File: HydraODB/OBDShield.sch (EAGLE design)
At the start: 29 parts, among them IC1 LM317MABDT, J1 HYDRABUS_SHIELD_CON_HEADER_2X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, J2 HYDRABUS_SHIELD_CON_HEADER_2X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, J3 HYDRABUS_SHIELD_CON_HEADER_2X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, K1 TS-1101F, U1 SN65HVD233DG4, U2 SN65HVD233DG4

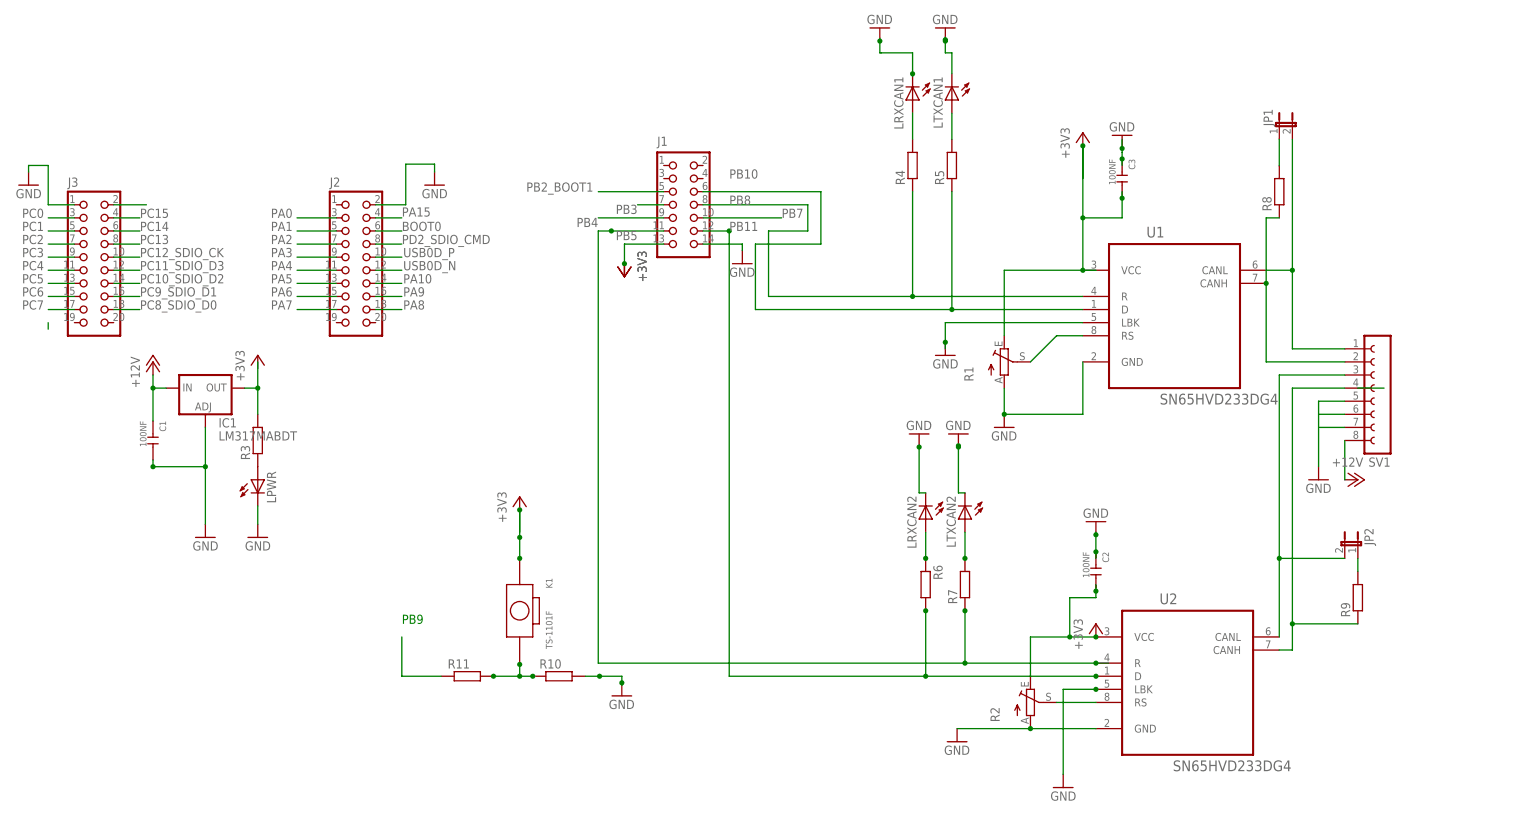
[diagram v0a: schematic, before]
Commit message: Power changed and jumper added, packages changed, inverted can h/l on silk
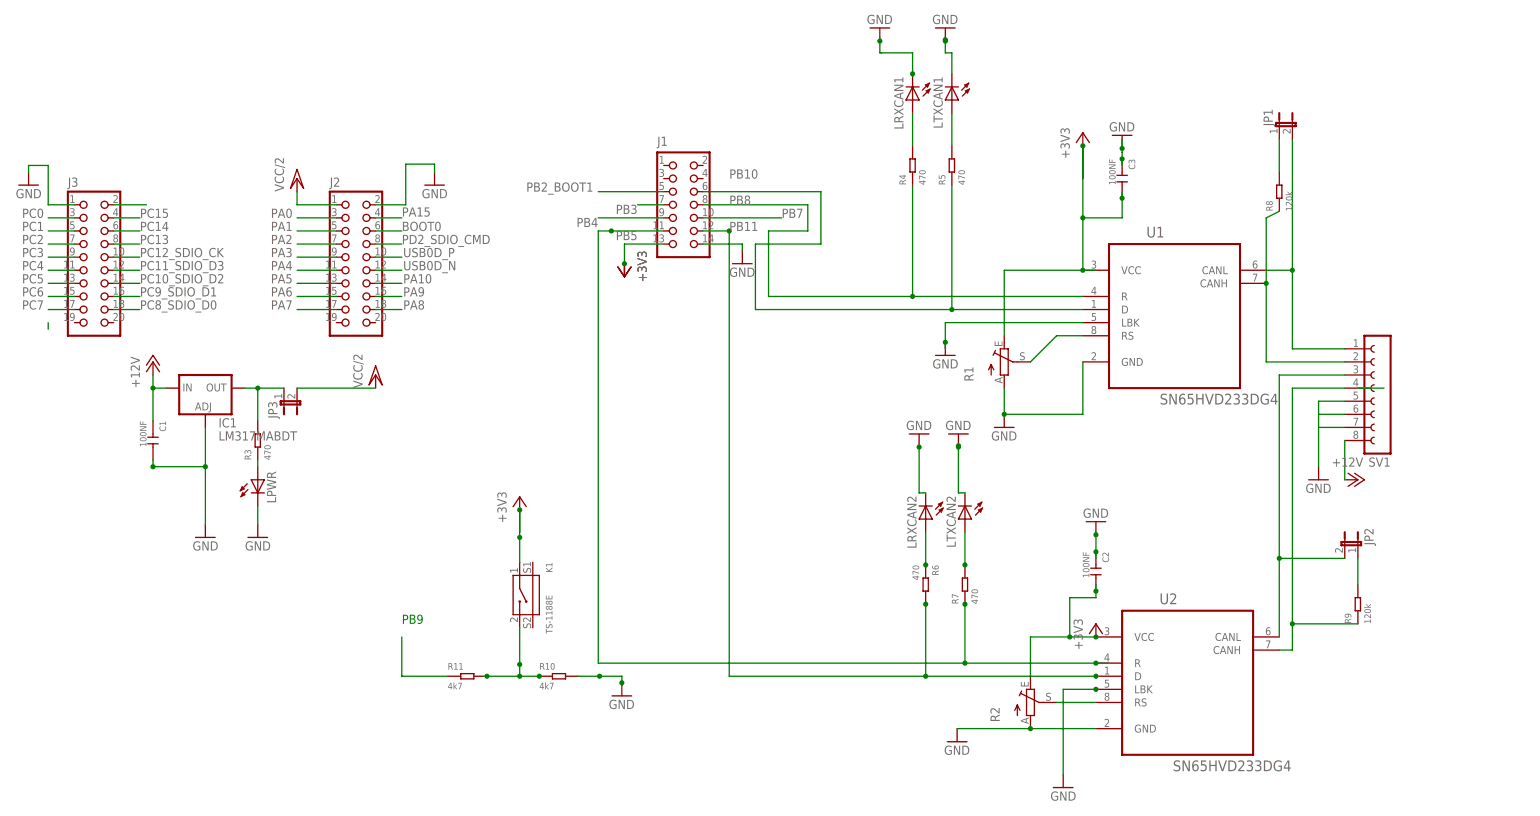
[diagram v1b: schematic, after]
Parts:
- added JP3: (no value), jumper:JP1E
- K1: value TS-1101F -> TS-1188E; device Seeed-OPL-Button:DIP-BUTTON-FRONT-WHITE(2P-3.4X6MM) -> Seeed-OPL-Button:SMD-BUTTON-2+2P
- R10, R11: value (none) -> 4k7; device resistor:R-EU_R0603 -> Seeed-OPL-Resistor:SMD-RES-33K-1%-1/4W(1206)
- R3, R4, R5, R6, R7: value (none) -> 470; device resistor:R-EU_R0603 -> Seeed-OPL-Resistor:SMD-RES-33K-1%-1/4W(1206)
- R8, R9: value (none) -> 120k; device resistor:R-EU_R0603 -> Seeed-OPL-Resistor:SMD-RES-33K-1%-1/4W(1206)
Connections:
- new net VCC/2: J2.1, JP3.2
- net N$15: now also JP3.1
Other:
- moved on the sheet: R9

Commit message: OBD Connector corrected, VReg changed, Routing modification and smd packages corrected
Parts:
- removed IC1: LM317MABDT, v-reg:LM317MABDT
- removed JP3: (no value), jumper:JP1E
- removed LPWR: (no value), led:LEDCHIPLED_0603
- removed SV1: (no value), con-lsta:FE08-1
- added C4: 33NF, Seeed-OPL-Capacitor:CERAMIC-100NF-50V-20%-Y5V(0805)
- added CN1: 8p-2.54, Seeed-OPL-Connector:DIP-BLACK-FEMALE-HEADER-VERT(8P-2.54)
- added J_USB: (no value), jumper:JP1E
- added PWR: (no value), led:LEDCHIPLED_0603
- added TC1, TC2, TVCC: TPB2,54, testpad:TPB2,54
- added U3: CJ78M05-to252, Seeed-OPL-ic:PMIC-CJ78M05(TO-252)
- renumbered JP1 to CAN1, JP2 to CAN2, LRXCAN1 to RX1, LRXCAN2 to RX2, LTXCAN1 to LX1, LTXCAN2 to TX2
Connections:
- net +12V: now also CN1.8, U3.IN; no longer IC1.IN, SV1.8
- net GND: now also C4.2, CN1.5, CN1.6, CN1.7, PWR.C, TC1.TP, TC2.TP, U3.GND; no longer IC1.ADJ, LPWR.C, SV1.5, SV1.6, SV1.7
- net N$10: now also CN1.2; no longer SV1.2
- net N$11: now also CN1.3; no longer SV1.3
- net N$12: now also CN1.4; no longer SV1.4
- net N$14: now also PWR.A; no longer LPWR.A
- net N$15: now also C4.1, J_USB.1, U3.OUT; no longer IC1.OUT, JP3.1
- net N$9: now also CN1.1; no longer SV1.1
- net VCC/2: now also J_USB.2, TVCC.TP; no longer JP3.2
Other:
- moved on the sheet: C1, R3, R8

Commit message: final working routing,
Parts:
- removed LX1, PWR, RX1, RX2, TX2: (no value), led:LEDCHIPLED_0603
- removed R3, R4, R5, R6, R7: 470, Seeed-OPL-Resistor:SMD-RES-33K-1%-1/4W(1206)
- removed TC2: TPB2,54, testpad:TPB2,54
- R1, R2: device pot:TRIM_EU-B25U -> pot:TRIM_EU-SM-42/43A
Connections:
- removed net N$13: LX1.A, R5.2
- removed net N$14: PWR.A, R3.1
- removed net N$4: R6.1, RX2.A
- removed net N$6: R7.2, TX2.A
- removed net N$7: R4.2, RX1.A
- removed net PA7: J2.17
- net GND: no longer LX1.C, PWR.C, RX1.C, RX2.C, TC2.TP, TX2.C
- net N$15: no longer R3.2
- net PB10: no longer R5.1
- net PB11: no longer R6.2
- net PB5: no longer R7.1
- net PB8: no longer R4.1
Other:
- moved on the sheet: CN1
